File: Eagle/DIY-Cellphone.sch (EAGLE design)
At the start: 64 parts, among them IC1 MEGA1284, J1 ISP, U1 MCP73831, U7 M10_HDWITHOUT_EXCLUSION, X1 BU-SMA-V, X3 CCM03-3002 R102

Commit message: New supercap.
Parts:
- U$4: value SUPERCAP -> SUPERCAPPAS; device cellphone:SUPERCAP -> cellphone:SUPERCAPPAS
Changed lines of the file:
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@@
 <part name="R5" library="rcl" deviceset="R-US_" device="R1206" value="4.7K"/>
 <part name="R8" library="rcl" deviceset="R-US_" device="R1206"/>
-<part name="U$4" library="cellphone" deviceset="SUPERCAP" device=""/>
+<part name="U$4" library="cellphone" deviceset="SUPERCAP" device="PAS"/>
 <part name="8MHZ" library="fab" deviceset="CRYSTAL" device=""/>
 <part name="C14" library="rcl" deviceset="C-EU" device="C1206" value="18pF"/>

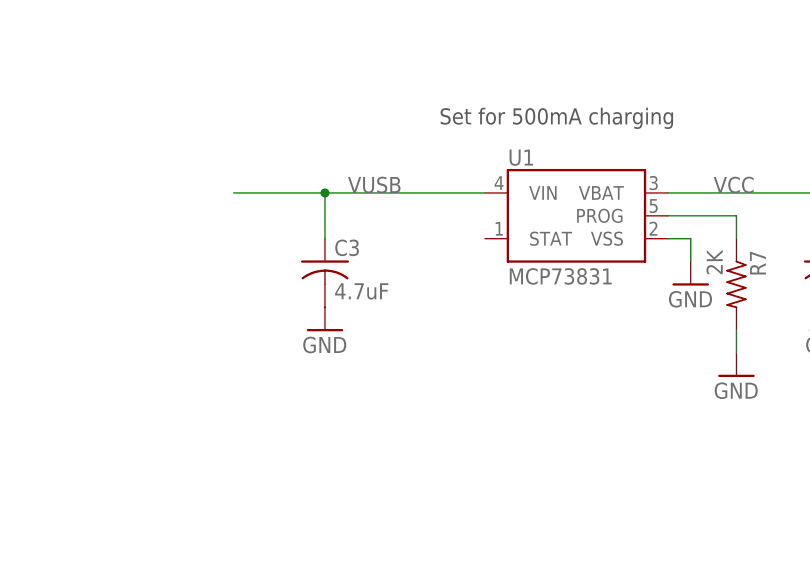
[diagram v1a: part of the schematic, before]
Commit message: Adding heat dissipation and LED on charging circuit.
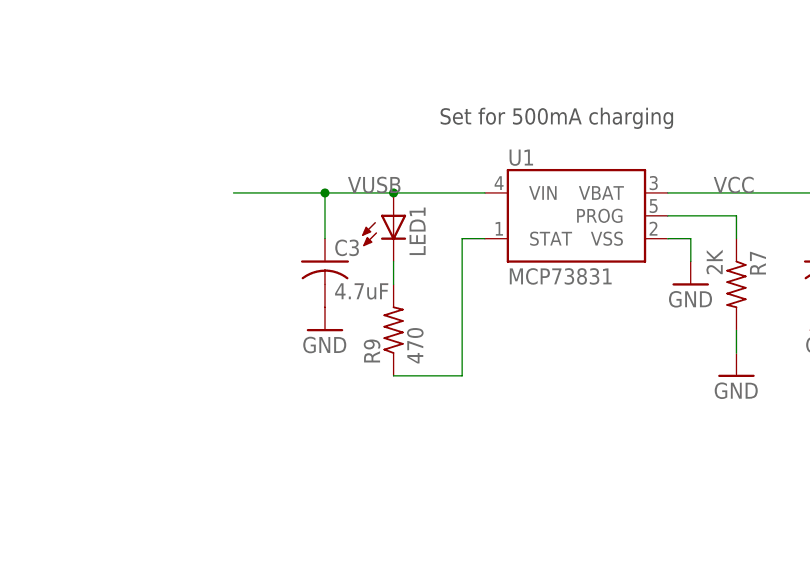
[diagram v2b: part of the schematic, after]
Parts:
- added LED1: (no value), led:LEDSMT1206
- added R9: 470, rcl:R-US_R1206
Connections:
- new net N$35: R9.1, U1.STAT
- new net N$36: LED1.C, R9.2
- net VUSB: now also LED1.A
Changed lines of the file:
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@@
 <part name="U$5" library="cellphone" deviceset="MINI-SIREN" device=""/>
 <part name="U$6" library="cellphone" deviceset="BUTTON-2" device=""/>
+<part name="R9" library="rcl" deviceset="R-US_" device="R1206" value="470"/>
+<part name="LED1" library="led" deviceset="LED" device="SMT1206"/>
 </parts>
 <sheets>
@@
 <instance part="U$5" gate="G$1" x="149.86" y="233.68" rot="R270"/>
 <instance part="U$6" gate="G$1" x="-66.04" y="109.22"/>
+<instance part="R9" gate="G$1" x="292.1" y="254" rot="R90"/>
+<instance part="LED1" gate="G$1" x="292.1" y="266.7"/>
 </instances>
 <busses>
@@
 <segment>
 <wire x1="284.48" y1="264.16" x2="284.48" y2="269.24" width="0.1524" layer="91"/>
-<wire x1="284.48" y1="269.24" x2="302.26" y2="269.24" width="0.1524" layer="91"/>
+<wire x1="284.48" y1="269.24" x2="292.1" y2="269.24" width="0.1524" layer="91"/>
+<wire x1="292.1" y1="269.24" x2="302.26" y2="269.24" width="0.1524" layer="91"/>
 <wire x1="274.32" y1="269.24" x2="284.48" y2="269.24" width="0.1524" layer="91"/>
 <junction x="284.48" y="269.24"/>
@@
 <pinref part="U1" gate="G$1" pin="VIN"/>
 <pinref part="C3" gate="G$1" pin="1"/>
+<pinref part="LED1" gate="G$1" pin="A"/>
+<junction x="292.1" y="269.24"/>
 </segment>
 <segment>
@@
 </segment>
 </net>
+<net name="N$35" class="0">
+<segment>
+<pinref part="U1" gate="G$1" pin="STAT"/>
+<pinref part="R9" gate="G$1" pin="1"/>
+<wire x1="292.1" y1="248.92" x2="299.72" y2="248.92" width="0.1524" layer="91"/>
+<wire x1="299.72" y1="248.92" x2="299.72" y2="264.16" width="0.1524" layer="91"/>
+<wire x1="299.72" y1="264.16" x2="302.26" y2="264.16" width="0.1524" layer="91"/>
+</segment>
+</net>
+<net name="N$36" class="0">
+<segment>
+<pinref part="R9" gate="G$1" pin="2"/>
+<wire x1="292.1" y1="259.08" x2="292.1" y2="261.62" width="0.1524" layer="91"/>
+<pinref part="LED1" gate="G$1" pin="C"/>
+</segment>
+</net>

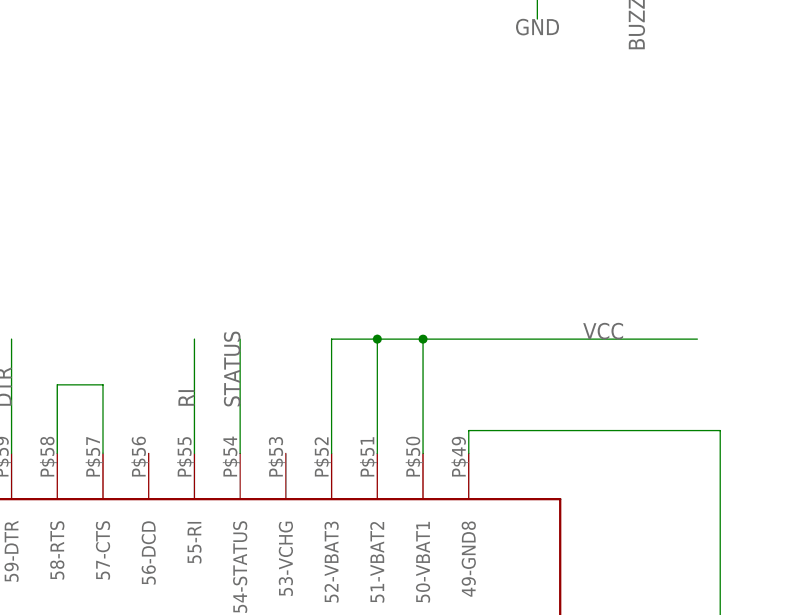
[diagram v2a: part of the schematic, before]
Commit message: Add LED on M10 status pin.
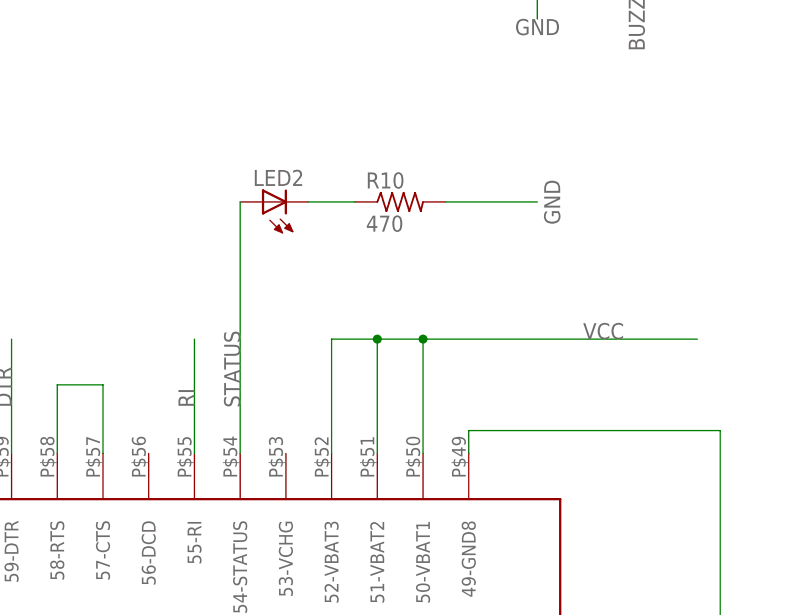
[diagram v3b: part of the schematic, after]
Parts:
- added LED2: (no value), led:LEDSMT1206
- added R10: 470, rcl:R-US_R1206
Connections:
- new net N$37: LED2.C, R10.1
- net GND: now also R10.2
- net STATUS: now also LED2.A
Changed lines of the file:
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@@
 <part name="R9" library="rcl" deviceset="R-US_" device="R1206" value="470"/>
 <part name="LED1" library="led" deviceset="LED" device="SMT1206"/>
+<part name="LED2" library="led" deviceset="LED" device="SMT1206"/>
+<part name="R10" library="rcl" deviceset="R-US_" device="R1206" value="470"/>
 </parts>
 <sheets>
@@
 <instance part="R9" gate="G$1" x="292.1" y="254" rot="R90"/>
 <instance part="LED1" gate="G$1" x="292.1" y="266.7"/>
+<instance part="LED2" gate="G$1" x="162.56" y="175.26" rot="R90"/>
+<instance part="R10" gate="G$1" x="177.8" y="175.26"/>
 </instances>
 <busses>
@@
 <pinref part="U$6" gate="G$1" pin="P"/>
 </segment>
+<segment>
+<pinref part="R10" gate="G$1" pin="2"/>
+<wire x1="182.88" y1="175.26" x2="193.04" y2="175.26" width="0.1524" layer="91"/>
+<label x="195.58" y="172.72" size="1.778" layer="95" rot="R90"/>
+</segment>
 </net>
 <net name="DISP_DATA" class="0">
@@
 <net name="STATUS" class="0">
 <segment>
-<wire x1="160.02" y1="147.32" x2="160.02" y2="160.02" width="0.1524" layer="91"/>
+<wire x1="160.02" y1="147.32" x2="160.02" y2="175.26" width="0.1524" layer="91"/>
 <label x="160.02" y="152.4" size="1.778" layer="95" rot="R90"/>
 <pinref part="U7" gate="G$1" pin="54-STATUS"/>
+<pinref part="LED2" gate="G$1" pin="A"/>
 </segment>
 <segment>
@@
 </segment>
 </net>
+<net name="N$37" class="0">
+<segment>
+<pinref part="LED2" gate="G$1" pin="C"/>
+<pinref part="R10" gate="G$1" pin="1"/>
+<wire x1="172.72" y1="175.26" x2="167.64" y2="175.26" width="0.1524" layer="91"/>
+</segment>
+</net>

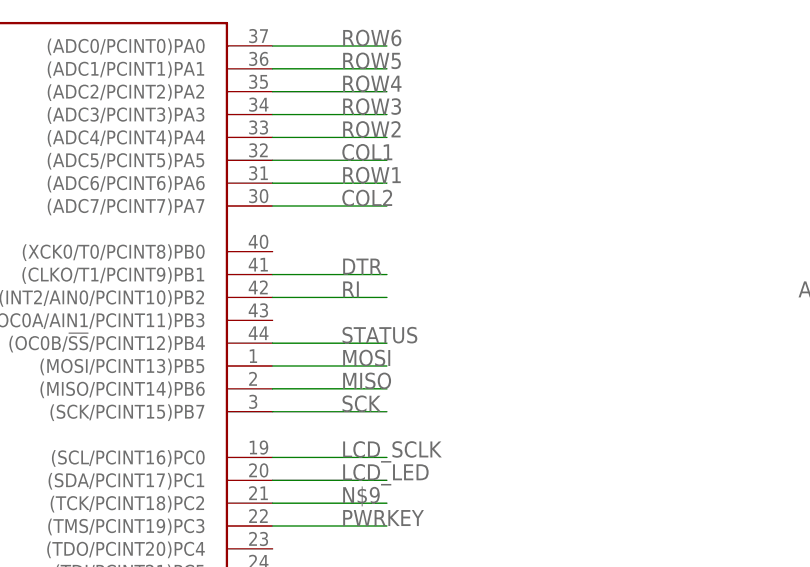
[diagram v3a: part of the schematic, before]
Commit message: Break out additional microcontroller pins.
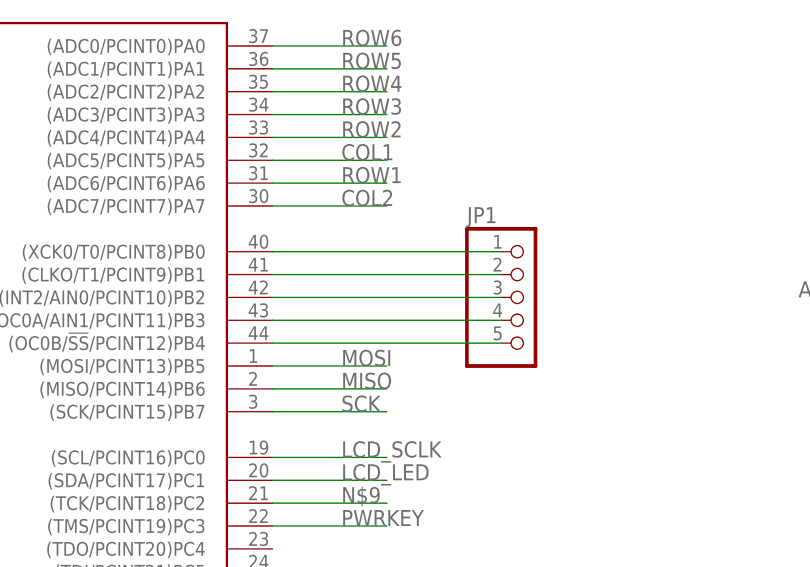
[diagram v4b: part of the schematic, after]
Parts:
- added JP1: (no value), pinhead:PINHD-1X5
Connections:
- new net N$38: IC1.(XCK0/T0/PCINT8)PB0, JP1.1
- new net N$39: IC1.(CLKO/T1/PCINT9)PB1, JP1.2
- new net N$40: IC1.(INT2/AIN0/PCINT10)PB2, JP1.3
- new net N$41: IC1.(OC0A/AIN1/PCINT11)PB3, JP1.4
- new net N$42: IC1.(OC0B/!SS!/PCINT12)PB4, JP1.5
- net DTR: no longer IC1.(CLKO/T1/PCINT9)PB1
- net RI: no longer IC1.(INT2/AIN0/PCINT10)PB2
- net STATUS: no longer IC1.(OC0B/!SS!/PCINT12)PB4
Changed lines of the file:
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@@
 <part name="LED2" library="led" deviceset="LED" device="SMT1206"/>
 <part name="R10" library="rcl" deviceset="R-US_" device="R1206" value="470"/>
+<part name="JP1" library="pinhead" deviceset="PINHD-1X5" device=""/>
 </parts>
 <sheets>
@@
 <instance part="LED2" gate="G$1" x="162.56" y="175.26" rot="R90"/>
 <instance part="R10" gate="G$1" x="177.8" y="175.26"/>
+<instance part="JP1" gate="A" x="33.02" y="81.28"/>
 </instances>
 <busses>
@@
 <pinref part="U7" gate="G$1" pin="59-DTR"/>
 </segment>
-<segment>
-<pinref part="IC1" gate="G$1" pin="(CLKO/T1/PCINT9)PB1"/>
-<wire x1="5.08" y1="83.82" x2="17.78" y2="83.82" width="0.1524" layer="91"/>
-<label x="12.7" y="83.82" size="1.778" layer="95"/>
-</segment>
 </net>
 <net name="GPIO0" class="0">
@@
 <pinref part="LED2" gate="G$1" pin="A"/>
 </segment>
-<segment>
-<pinref part="IC1" gate="G$1" pin="(OC0B/!SS!/PCINT12)PB4"/>
-<wire x1="5.08" y1="76.2" x2="17.78" y2="76.2" width="0.1524" layer="91"/>
-<label x="12.7" y="76.2" size="1.778" layer="95"/>
-</segment>
 </net>
 <net name="SIM_RSTR" class="0">
@@
 <pinref part="U7" gate="G$1" pin="55-RI"/>
 <label x="154.94" y="152.4" size="1.778" layer="95" rot="R90"/>
-</segment>
-<segment>
-<pinref part="IC1" gate="G$1" pin="(INT2/AIN0/PCINT10)PB2"/>
-<wire x1="5.08" y1="81.28" x2="17.78" y2="81.28" width="0.1524" layer="91"/>
-<label x="12.7" y="81.28" size="1.778" layer="95"/>
 </segment>
 </net>
@@
 </segment>
 </net>
+<net name="N$38" class="0">
+<segment>
+<pinref part="IC1" gate="G$1" pin="(XCK0/T0/PCINT8)PB0"/>
+<pinref part="JP1" gate="A" pin="1"/>
+<wire x1="30.48" y1="86.36" x2="5.08" y2="86.36" width="0.1524" layer="91"/>
+</segment>
+</net>
+<net name="N$39" class="0">
+<segment>
+<pinref part="IC1" gate="G$1" pin="(CLKO/T1/PCINT9)PB1"/>
+<pinref part="JP1" gate="A" pin="2"/>
+<wire x1="30.48" y1="83.82" x2="5.08" y2="83.82" width="0.1524" layer="91"/>
+</segment>
+</net>
+<net name="N$40" class="0">
+<segment>
+<pinref part="IC1" gate="G$1" pin="(INT2/AIN0/PCINT10)PB2"/>
+<pinref part="JP1" gate="A" pin="3"/>
+<wire x1="30.48" y1="81.28" x2="5.08" y2="81.28" width="0.1524" layer="91"/>
+</segment>
+</net>
+<net name="N$41" class="0">
+<segment>
+<pinref part="IC1" gate="G$1" pin="(OC0A/AIN1/PCINT11)PB3"/>
+<pinref part="JP1" gate="A" pin="4"/>
+<wire x1="30.48" y1="78.74" x2="5.08" y2="78.74" width="0.1524" layer="91"/>
+</segment>
+</net>
+<net name="N$42" class="0">
+<segment>
+<pinref part="IC1" gate="G$1" pin="(OC0B/!SS!/PCINT12)PB4"/>
+<pinref part="JP1" gate="A" pin="5"/>
+<wire x1="30.48" y1="76.2" x2="5.08" y2="76.2" width="0.1524" layer="91"/>
+</segment>
+</net>

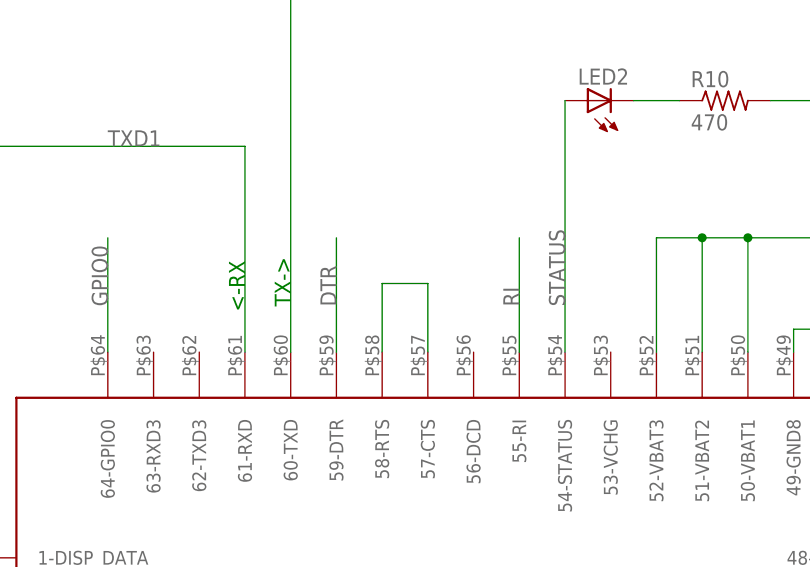
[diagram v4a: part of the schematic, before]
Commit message: Remove RTS/CTS connection on M10.
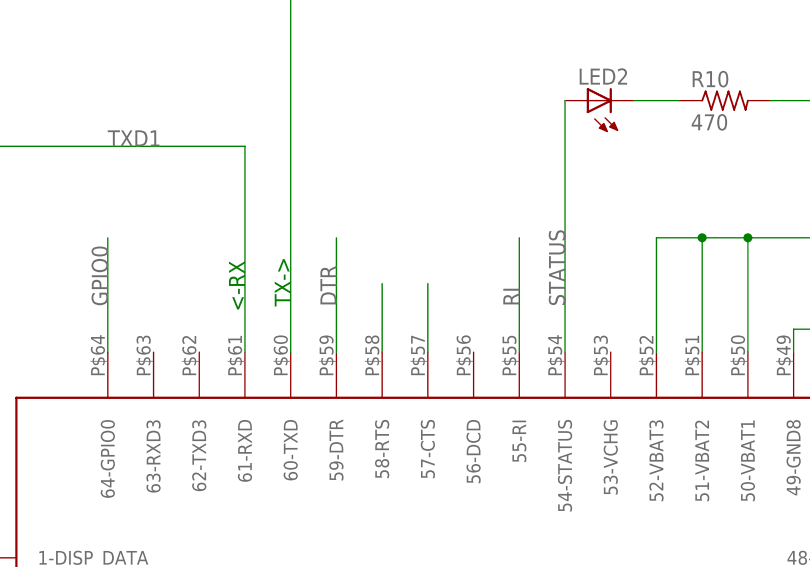
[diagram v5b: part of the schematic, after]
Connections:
- new net N$43: U7.58-RTS
- net N$1: no longer U7.58-RTS
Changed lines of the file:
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@@
 <segment>
 <wire x1="144.78" y1="147.32" x2="144.78" y2="154.94" width="0.1524" layer="91"/>
-<wire x1="144.78" y1="154.94" x2="139.7" y2="154.94" width="0.1524" layer="91"/>
-<wire x1="139.7" y1="154.94" x2="139.7" y2="147.32" width="0.1524" layer="91"/>
 <pinref part="U7" gate="G$1" pin="57-CTS"/>
-<pinref part="U7" gate="G$1" pin="58-RTS"/>
 </segment>
 </net>
@@
 </segment>
 </net>
+<net name="N$43" class="0">
+<segment>
+<wire x1="139.7" y1="154.94" x2="139.7" y2="147.32" width="0.1524" layer="91"/>
+<pinref part="U7" gate="G$1" pin="58-RTS"/>
+</segment>
+</net>

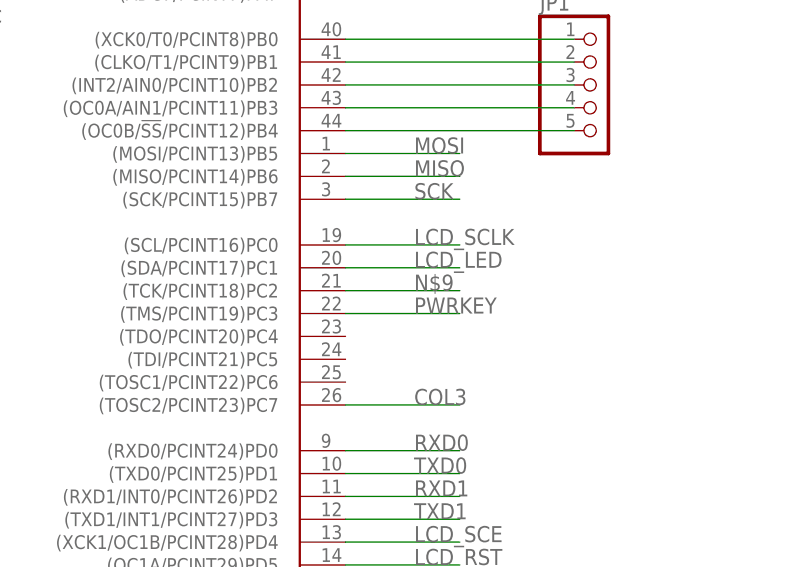
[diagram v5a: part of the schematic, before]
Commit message: Add buzzer hole. Align buzzer / reset button / speaker. Move some wires.
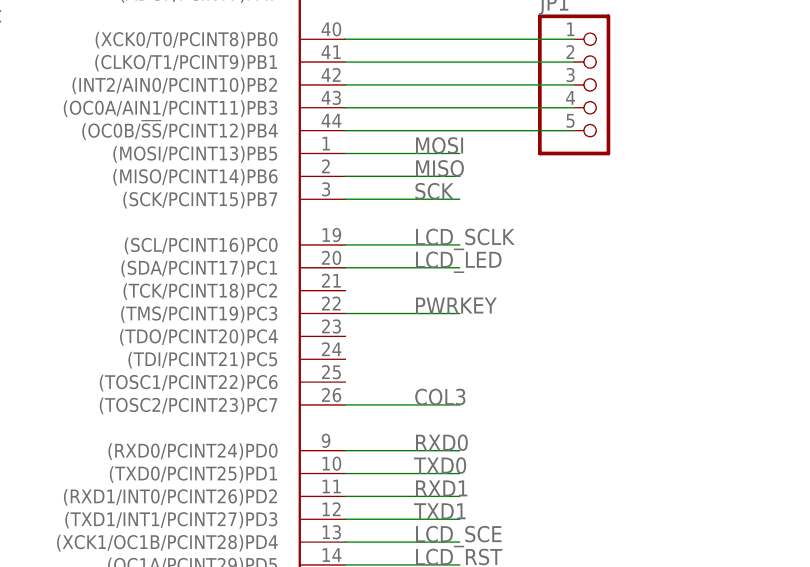
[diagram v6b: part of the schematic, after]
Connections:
- removed net N$9: IC1.(TCK/PCINT18)PC2
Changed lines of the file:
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@@
-</segment>
-</net>
-<net name="N$9" class="0">
-<segment>
-<pinref part="IC1" gate="G$1" pin="(TCK/PCINT18)PC2"/>
-<wire x1="5.08" y1="58.42" x2="17.78" y2="58.42" width="0.1524" layer="91"/>
-<label x="12.7" y="58.42" size="1.778" layer="95"/>
 </segment>
 </net>

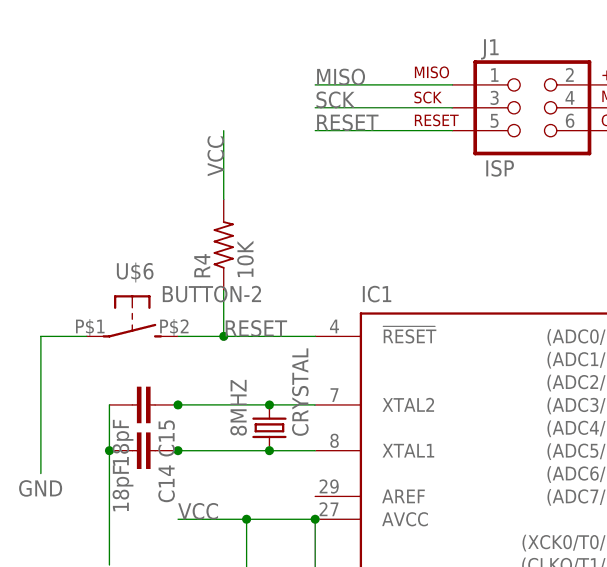
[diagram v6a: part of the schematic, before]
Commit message: Adjust silk-screen.
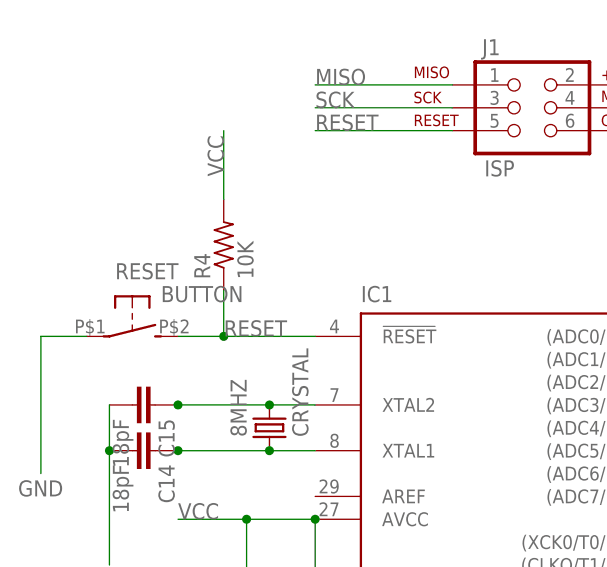
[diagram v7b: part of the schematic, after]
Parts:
- RESET: value BUTTON-2 -> BUTTON
- renumbered U$6 to RESET
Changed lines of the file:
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@@
 <part name="C16" library="rcl" deviceset="CPOL-US" device="D/7343-31R" value="1000uF"/>
 <part name="U$5" library="cellphone" deviceset="MINI-SIREN" device=""/>
-<part name="U$6" library="cellphone" deviceset="BUTTON-2" device=""/>
+<part name="RESET" library="cellphone" deviceset="BUTTON-2" device="" value="BUTTON"/>
 <part name="R9" library="rcl" deviceset="R-US_" device="R1206" value="470"/>
 <part name="LED1" library="led" deviceset="LED" device="SMT1206"/>
@@
 <instance part="C16" gate="G$1" x="302.26" y="213.36"/>
 <instance part="U$5" gate="G$1" x="149.86" y="233.68" rot="R270"/>
-<instance part="U$6" gate="G$1" x="-66.04" y="109.22"/>
+<instance part="RESET" gate="G$1" x="-66.04" y="109.22"/>
 <instance part="R9" gate="G$1" x="292.1" y="254" rot="R90"/>
 <instance part="LED1" gate="G$1" x="292.1" y="266.7"/>
@@
 <label x="-78.74" y="91.44" size="1.778" layer="95"/>
 <wire x1="-76.2" y1="109.22" x2="-71.12" y2="109.22" width="0.1524" layer="91"/>
-<pinref part="U$6" gate="G$1" pin="P"/>
+<pinref part="RESET" gate="G$1" pin="P"/>
 </segment>
 <segment>
@@
 <wire x1="-55.88" y1="109.22" x2="-60.96" y2="109.22" width="0.1524" layer="91"/>
 <junction x="-55.88" y="109.22"/>
-<pinref part="U$6" gate="G$1" pin="S"/>
-</segment>
-<segment>
+<pinref part="RESET" gate="G$1" pin="S"/>
+</segment>
+<segment>
